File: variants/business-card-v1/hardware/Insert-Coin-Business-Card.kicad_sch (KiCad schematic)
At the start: 49 parts, among them J1 Conn_01x02, Q1 CJ3400, Q10 CJ3400, Q2 CJ3400, Q3 CJ3400, Q4 CJ3400, Q5 CJ3400, Q7 CJ3400, Q8 CJ3400, Q9 CJ3400, U1 ATtiny1616-M, U2 ST25DV04K-IER8C3

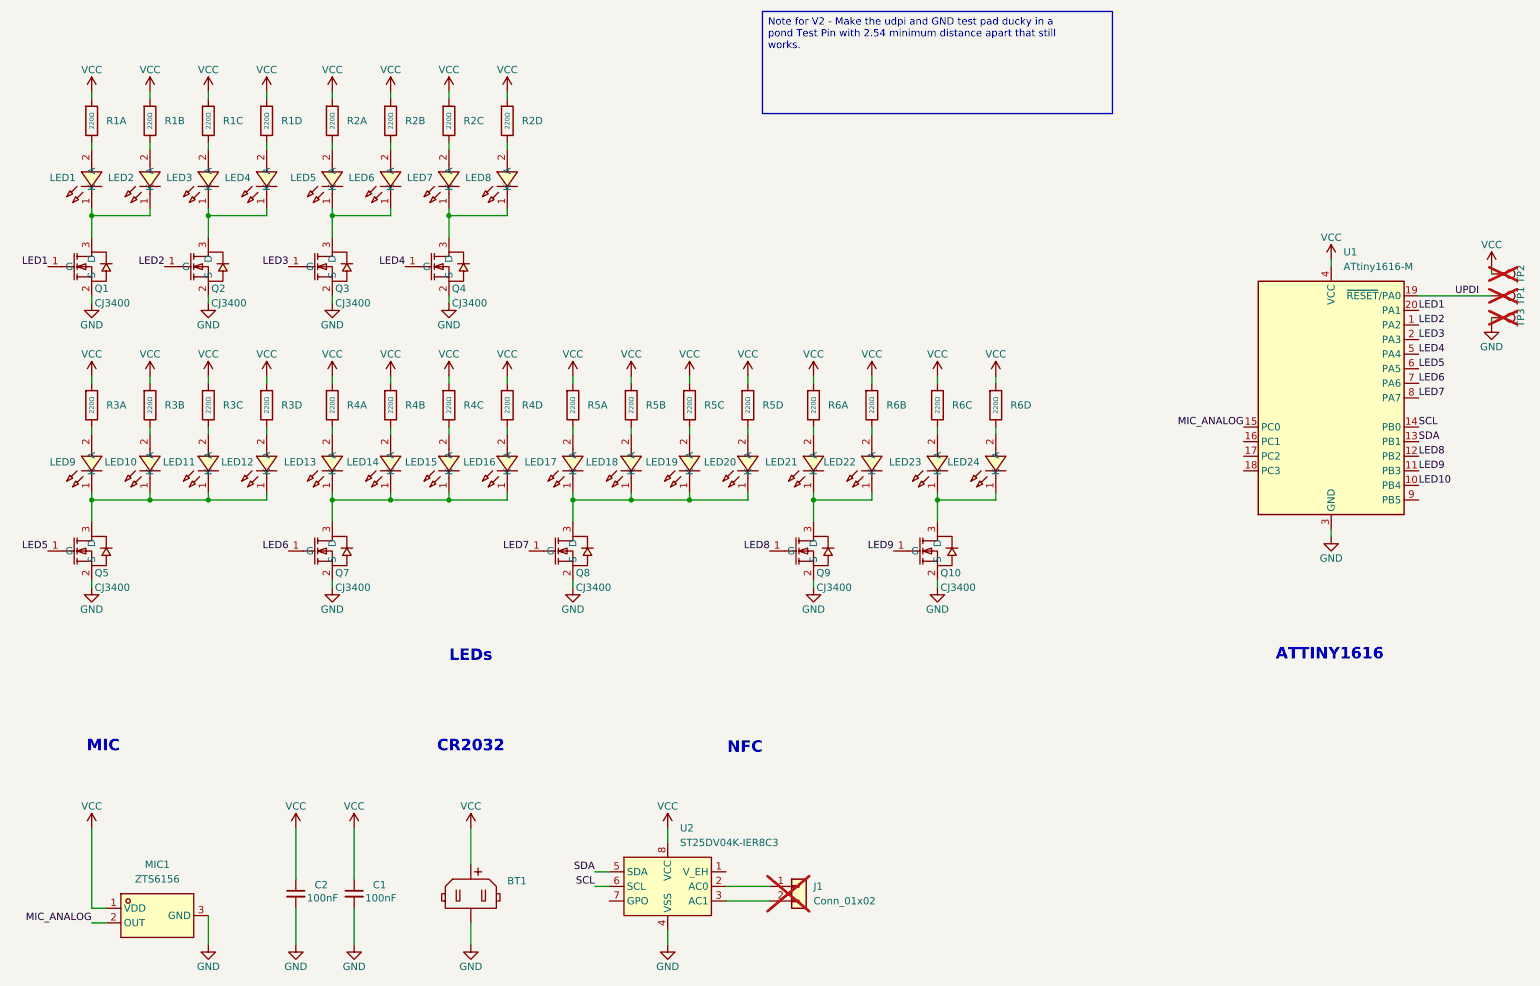
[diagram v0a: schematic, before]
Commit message: PCB File Updated
- updated the pcb layout and mic choice to have it be economy parts for jlc.
- removed the VCC testpoint
- change UPDI & GND testpoint to be ducky shape
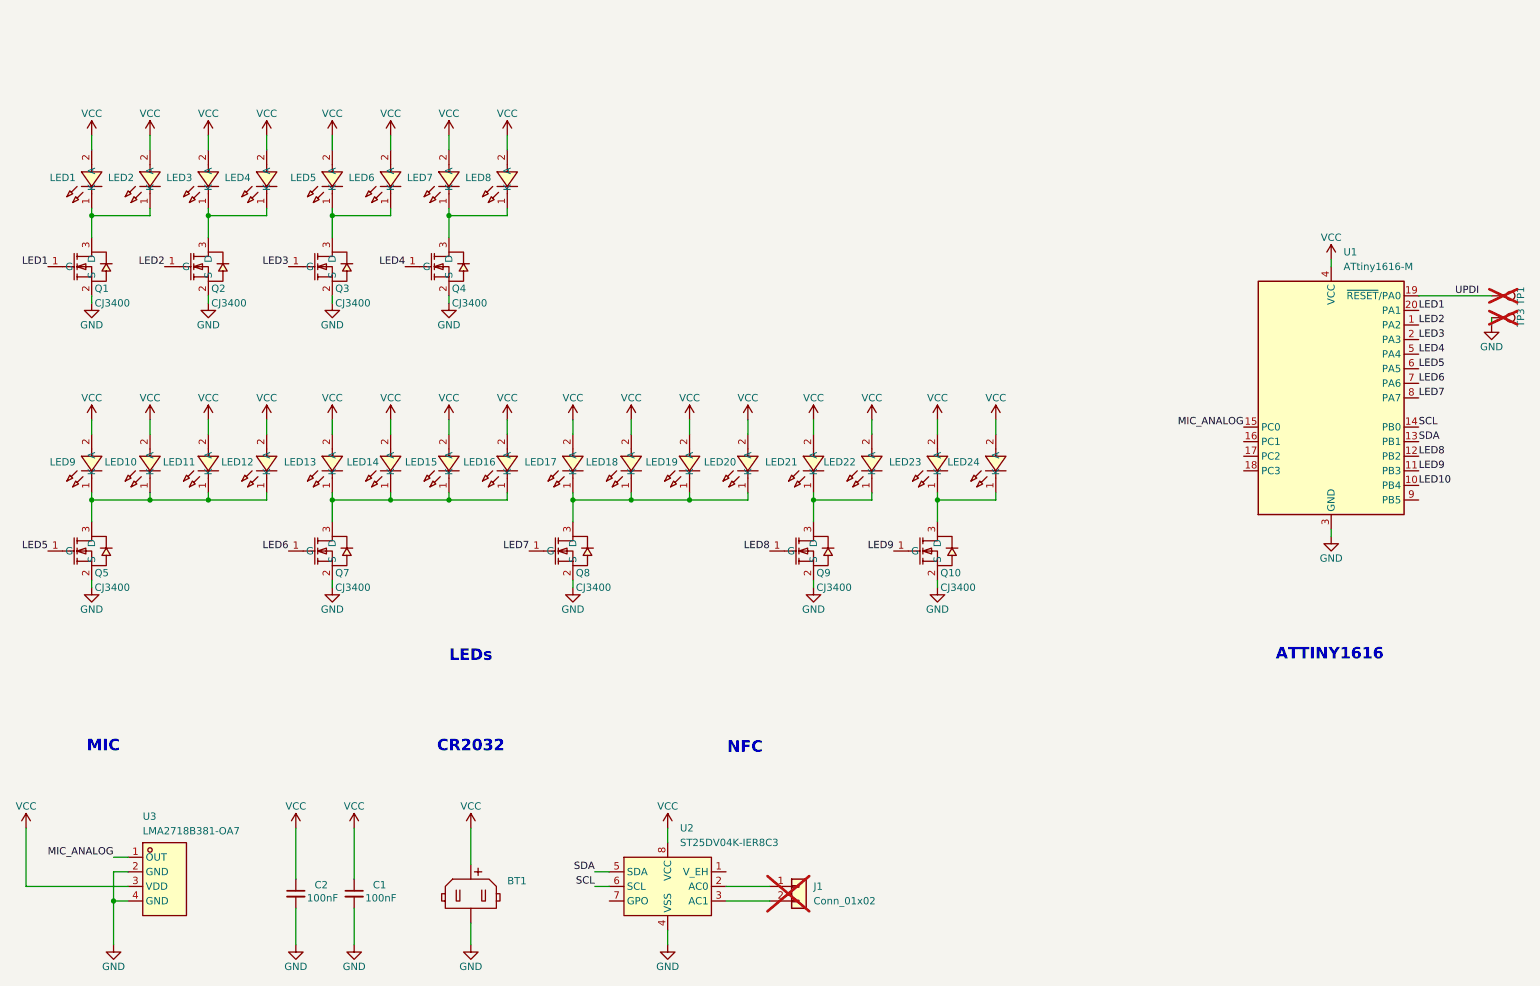
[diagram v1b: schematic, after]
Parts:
- removed MIC1: ZTS6156, KiCadPartFinder:MIC-SMD_3P-L2.8-W1.9_ZTS6056, symbol KiCadPartFinder:ZTS6156
- removed R1, R2, R3, R4, R5, R6: 220Ω, PCM_Resistor_SMD_AKL:R_Array_Convex_4x0402, symbol PCM_JLCPCB-Resistors:0402x4,10kΩ
- removed TP2: 1.0mm, PCM_SparkFun-Connector:TestPoint-1.0mm, symbol PCM_SparkFun-Connector:TestPoint_1.0mm
- added U3: LMA2718B381-OA7, KiCadPartFinder:MIC-SMD_4P-L2.8-W1.9_LMA2718B381-OA7, symbol KiCadPartFinder:LMA2718B381-OA7
- TP1, TP3: footprint PCM_SparkFun-Connector:TestPoint-1.0mm -> DavidLib_Graphics:DUCKY_ICON_2.54_Spacing
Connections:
- net GND: now also U3.2 (GND), U3.4 (GND)
- net MIC_ANALOG: now also U3.1 (OUT)
- net VCC: now also LED1.2 (A), LED10.2 (A), LED11.2 (A), LED12.2 (A), LED13.2 (A), LED14.2 (A), LED15.2 (A), LED16.2 (A), LED17.2 (A), LED18.2 (A), LED19.2 (A), LED2.2 (A), LED20.2 (A), LED21.2 (A), LED22.2 (A), LED23.2 (A), LED24.2 (A), LED3.2 (A), LED4.2 (A), LED5.2 (A), LED6.2 (A), LED7.2 (A), LED8.2 (A), LED9.2 (A), U3.3 (VDD)
